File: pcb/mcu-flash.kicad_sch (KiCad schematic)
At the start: 31 parts, among them J1 0015910100, J4 BM03B-SRSS-TB, SW1 EVQ-P7J01P, SW2 TS04-66-50-BK-160-SMT, U1 W25Q128JVS, U2 RP2040, Y1 ABM8AIG-12.000MHZ-12-2Z-T3

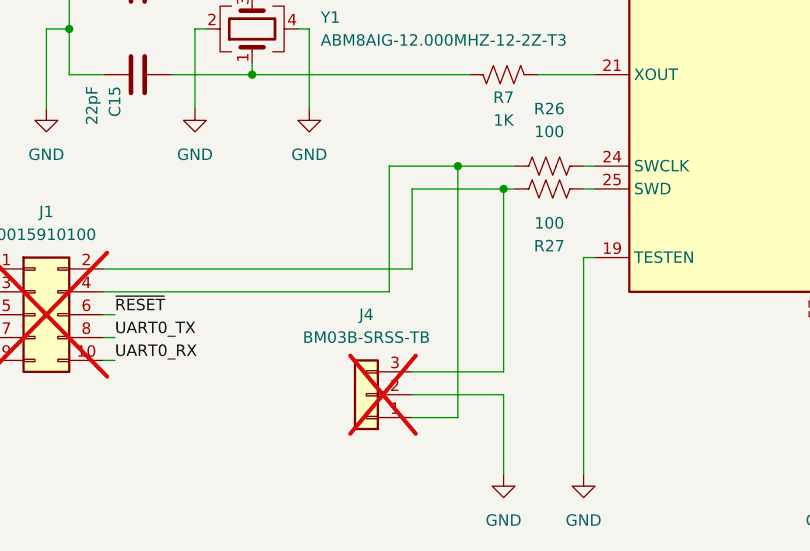
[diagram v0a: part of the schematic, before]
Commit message: Address PCB issues found during testing
- Switch motor connector to JST PH
- Remove AIN_REF connection on TMC2130
- Replace sense resistors with 0.5 Ohm
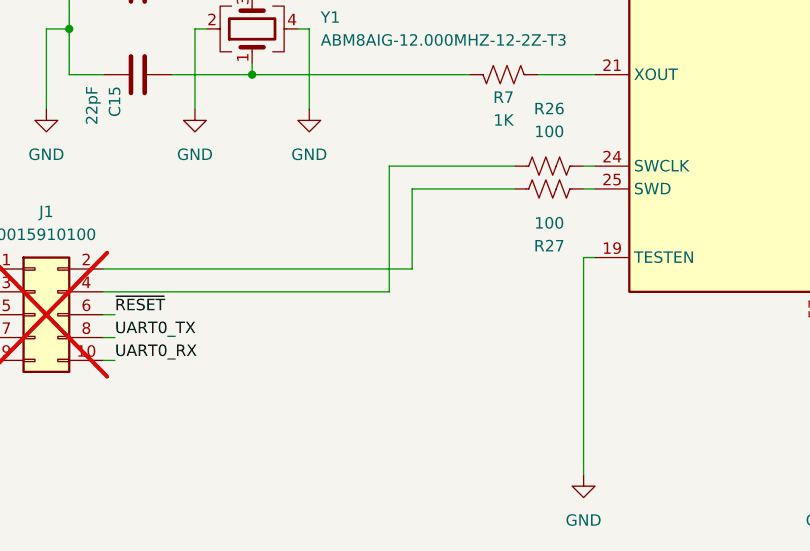
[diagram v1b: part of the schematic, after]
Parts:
- removed J4: BM03B-SRSS-TB, Connector_JST:JST_SH_BM03B-SRSS-TB_1x03-1MP_P1.00mm_Vertical, symbol Connector_Generic:Conn_01x03
- SW2: footprint open-ephys:SAMESKY-TS04-66-XX-BK-XXX-SMT-XX -> open-ephys:SAMESKY_TS04-66-XX-BK-XXX-SMT-XX
